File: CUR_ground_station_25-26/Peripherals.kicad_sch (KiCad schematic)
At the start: 0 parts

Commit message: added user stuff
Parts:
- added BZ1: CMT-1209-390T, symbol Device:Buzzer
- added D1: D_Schottky, symbol Device:D_Schottky
- added Led_1, Led_2, Led_3: CLV1L-FKB, LED_SMD:LED_Cree-PLCC4_3.2x2.8mm_CCW, symbol LED:CLV1L-FKB
- added Q1: NTR4003N, symbol Transistor_FET:Q_NMOS_GSD
- added R1, R10, R11, R2, R7, R8: 22, symbol Device:R_Small_US
- added R3, R5, R6, R9: 150, symbol Device:R_Small_US
- added R4: 10k, symbol Device:R_Small_US
- added SW1, SW2, SW3, SW4: SW_Push, symbol Switch:SW_Push
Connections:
- new net: Led_3.2 (RK), R9.1
- new net: Led_1.4 (BK), R2.1
- new net: Led_3.3 (GK), R10.1
- new net: Led_3.4 (BK), R11.1
- new net: Led_2.2 (RK), R6.1
- new net: Q1.1 (G), R4.1, R5.2
- new net: BZ1.2 (-), D1.2 (A), Q1.3 (D)
- new net: Led_2.4 (BK), R8.1
- new net: Led_2.3 (GK), R7.1
- new net: Led_1.2 (RK), R3.1
- new net: Led_1.3 (GK), R1.1
- new net +3V3: BZ1.1 (+), D1.1 (K), Led_1.1 (A), Led_2.1 (A), Led_3.1 (A), SW1.2, SW2.2, SW3.2, SW4.2
- new net BTN_1: SW1.1, SW2.1, SW3.1, SW4.1
- new net Buzzer: R5.1
- new net GND: Q1.2 (S), R4.2
- new net LED_1_B: R2.2
- new net LED_1_G: R1.2
- new net LED_1_R: R3.2
- new net LED_2_B: R8.2
- new net LED_2_G: R7.2
- new net LED_2_R: R6.2
- new net LED_3_B: R11.2
- new net LED_3_G: R10.2
- new net LED_3_R: R9.2
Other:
- note added: "Aiming for around 5ma"
- note added: "Blue: 3.1"
- note added: "Button"
- note added: "Buzzer"
- note added: "Forward Voltages"
- note added: "Green: 3.1"
- note added: "LED"
- note added: "Red: 2.6"

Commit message: added buncha stuff from flight computer
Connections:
- net BTN_1: no longer SW2.1, SW3.1, SW4.1
- new net BTN_2: SW2.1
- new net BTN_3: SW3.1
- new net BTN_4: SW4.1
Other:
- moved on the sheet: BZ1, D1, Led_1, Led_2, Led_3, Q1, R1, R10, R11, R2, R3, R4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

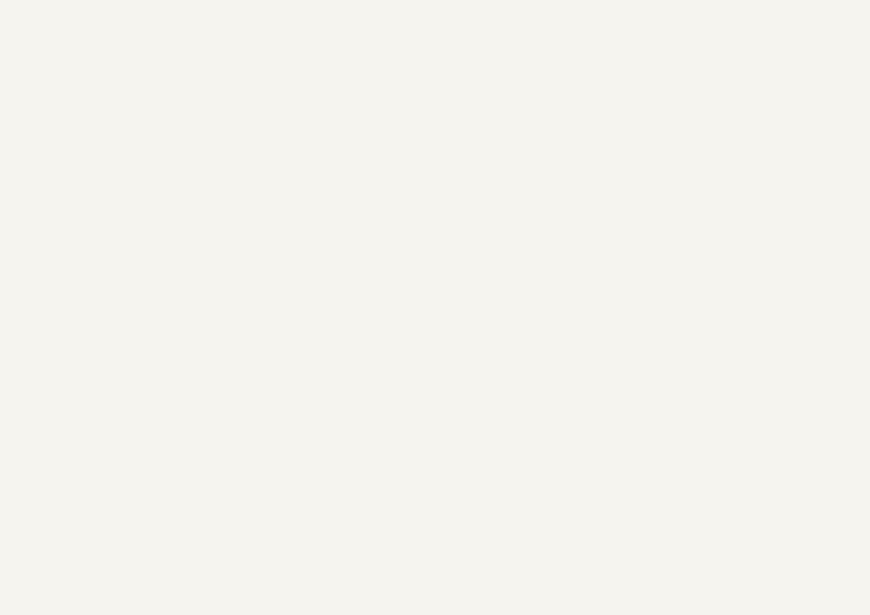
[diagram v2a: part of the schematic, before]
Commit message: Add epaper
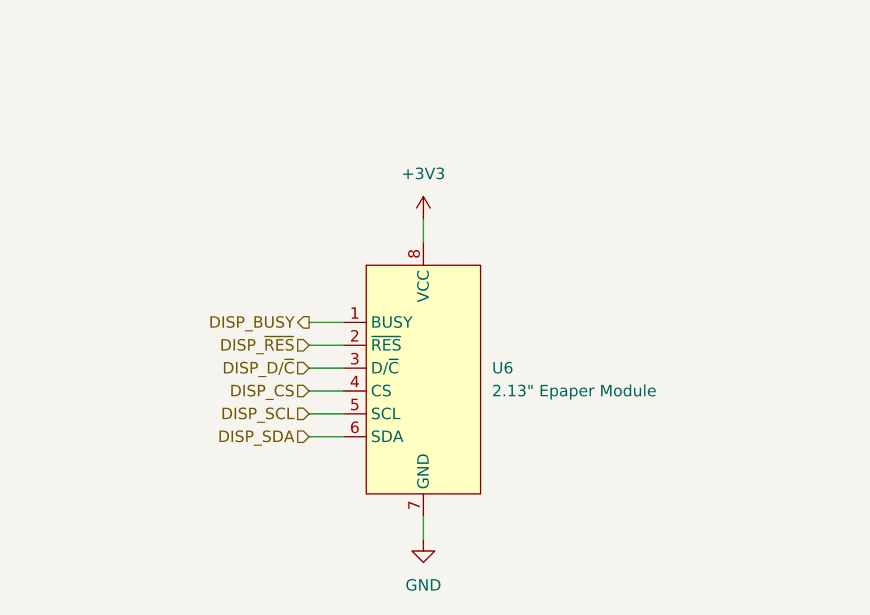
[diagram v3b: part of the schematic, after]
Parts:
- added U6: 2.13" Epaper Module, WeAct-Studio-2.13-Epaper:WeAct-Studio-2.13-Epaper, symbol WeAct-Studio-Epaper:WeAct-Studio-2.13-Epaper
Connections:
- net +3V3: now also U6.8 (VCC)
- net GND: now also U6.7 (GND)
- new net DISP_BUSY: U6.1 (BUSY)
- new net DISP_CS: U6.4 (CS)
- new net DISP_D/~{C}: U6.3 (D/~{C})
- new net DISP_SCL: U6.5 (SCL)
- new net DISP_SDA: U6.6 (SDA)
- new net DISP_~{RES}: U6.2 (~{RES})

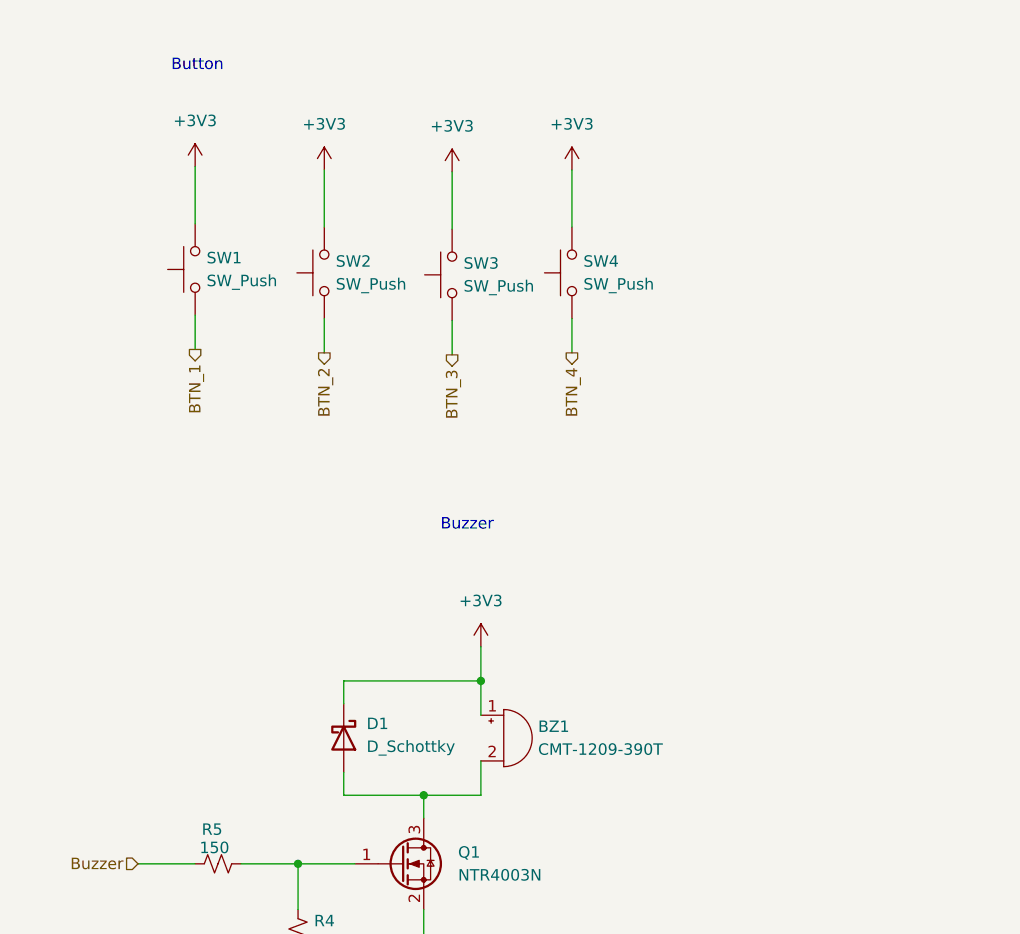
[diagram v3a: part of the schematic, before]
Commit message: Cleanup UI sheet
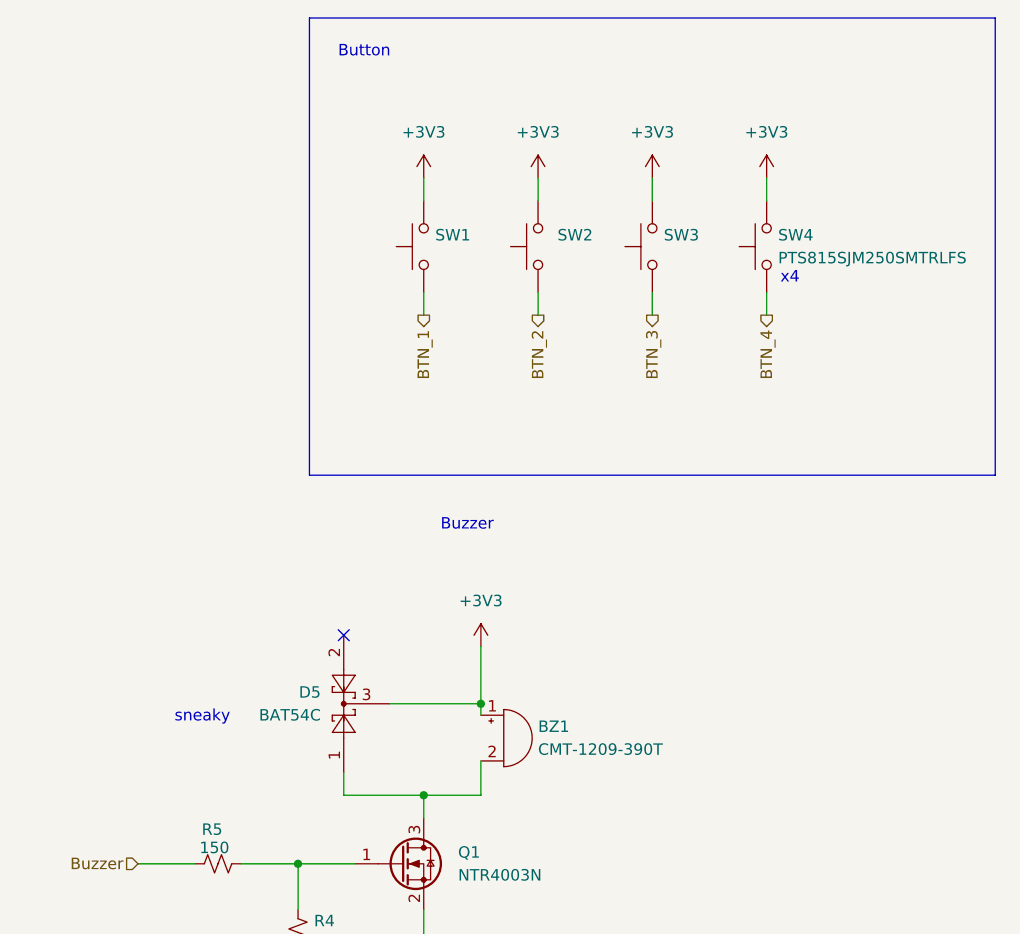
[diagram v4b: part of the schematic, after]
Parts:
- removed D1: D_Schottky, symbol Device:D_Schottky
- added D5: BAT54C, Package_TO_SOT_SMD:SOT-23, symbol Diode:BAT54C
- SW1, SW2, SW3, SW4: value SW_Push -> PTS815SJM250SMTRLFS
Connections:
- net +3V3: now also D5.3
- net at BZ1.2 (-), Q1.3 (D): now also D5.1
- no-connect marks 0 -> 1
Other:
- note added: "sneaky"
- note added: "x4"
- moved on the sheet: SW1, SW2, SW3, SW4

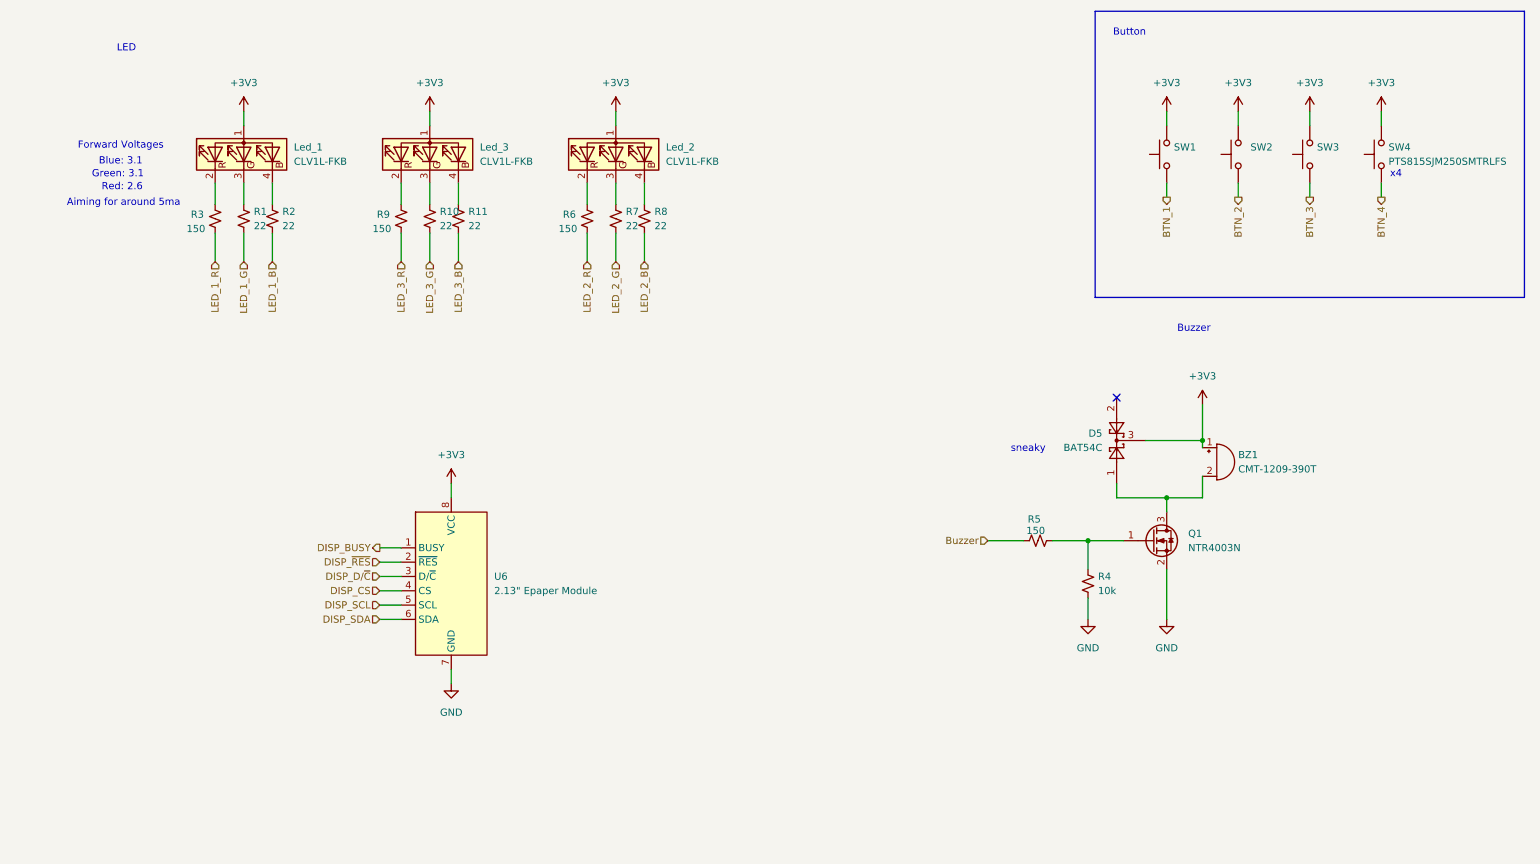
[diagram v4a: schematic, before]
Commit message: Cleanup peripherals again
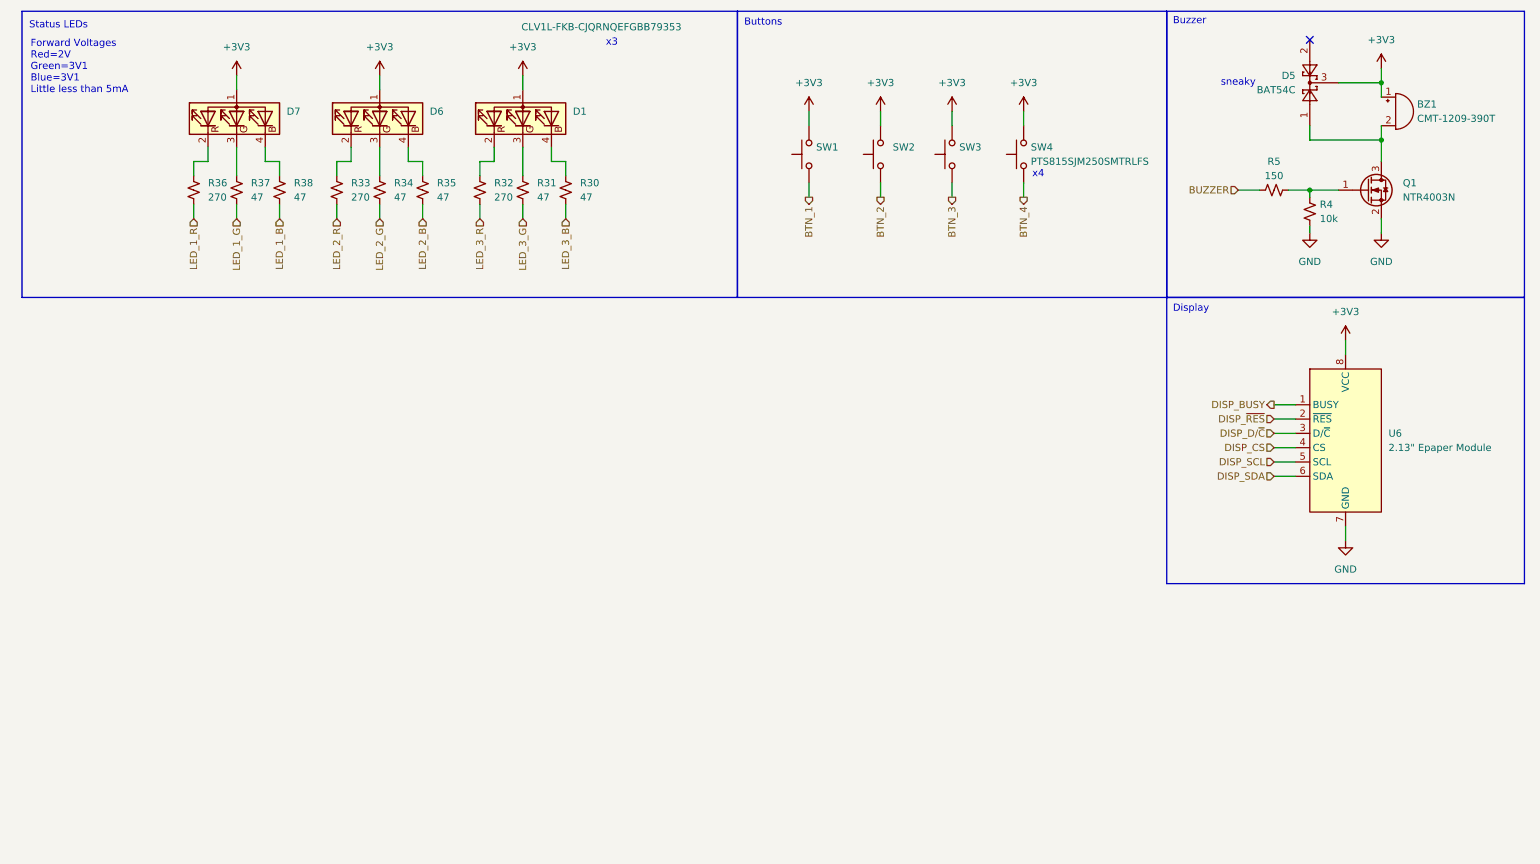
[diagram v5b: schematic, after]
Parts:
- removed Led_1, Led_2, Led_3: CLV1L-FKB, LED_SMD:LED_Cree-PLCC4_3.2x2.8mm_CCW, symbol LED:CLV1L-FKB
- removed R1, R10, R11, R2, R7, R8: 22, symbol Device:R_Small_US
- removed R3, R6, R9: 150, symbol Device:R_Small_US
- added D1, D6, D7: CLV1L-FKB-CJQRNQEFGBB79353, LED_SMD:LED_Cree-PLCC4_3.2x2.8mm_CCW, symbol Device:LED_ARGB
- added R30, R31, R34, R35, R37, R38: 47, symbol Device:R_Small_US
- added R32, R33, R36: 270, symbol Device:R_Small_US
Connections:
- net +3V3: now also D1.1 (A), D6.1 (A), D7.1 (A)
- net LED_1_B: now also R38.2
- net LED_1_G: now also R37.2
- net LED_1_R: now also R36.2
- net LED_2_B: now also R35.2
- net LED_2_G: now also R34.2
- net LED_2_R: now also R33.2
- net LED_3_B: now also R30.2
- net LED_3_G: now also R31.2
- net LED_3_R: now also R32.2
- net Buzzer renamed BUZZER
- new net: D1.4 (BK), R30.1
- new net: D1.2 (RK), R32.1
- new net: D7.2 (RK), R36.1
- new net: D7.3 (GK), R37.1
- new net: D7.4 (BK), R38.1
- new net: D6.3 (GK), R34.1
- new net: D1.3 (GK), R31.1
- new net: D6.4 (BK), R35.1
- new net: D6.2 (RK), R33.1
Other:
- note added: "Buttons"
- note added: "Display"
- note added: "Forward Voltages Red=2V Green=3V1 Blue=3V1 Little less than 5mA"
- note added: "Status LEDs"
- note added: "x3"
- note removed: "Aiming for around 5ma"
- note removed: "Blue: 3.1"
- note removed: "Button"
- note removed: "Forward Voltages"
- note removed: "Green: 3.1"
- note removed: "LED"
- note removed: "Red: 2.6"
- moved on the sheet: BZ1, D5, Q1, R4, R5, SW1, SW2, SW3, SW4, U6

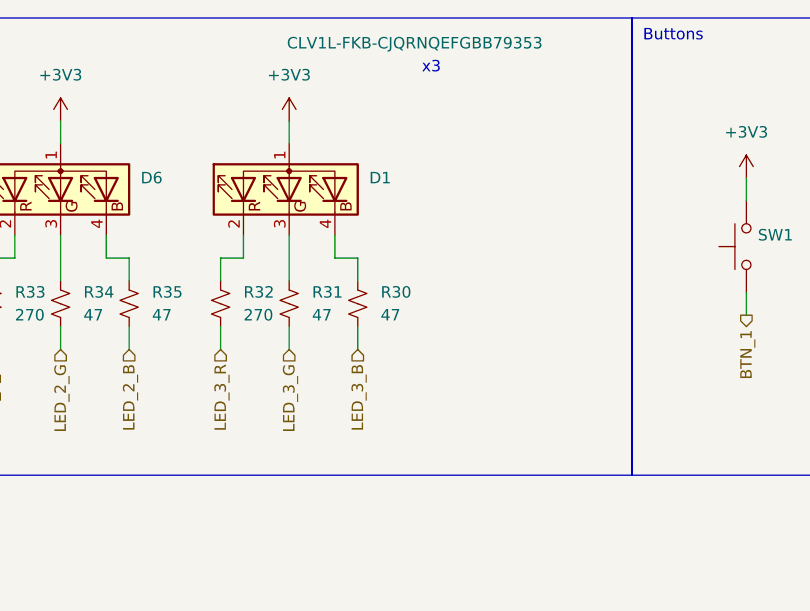
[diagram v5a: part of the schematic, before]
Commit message: Change MCU, hookup more pins
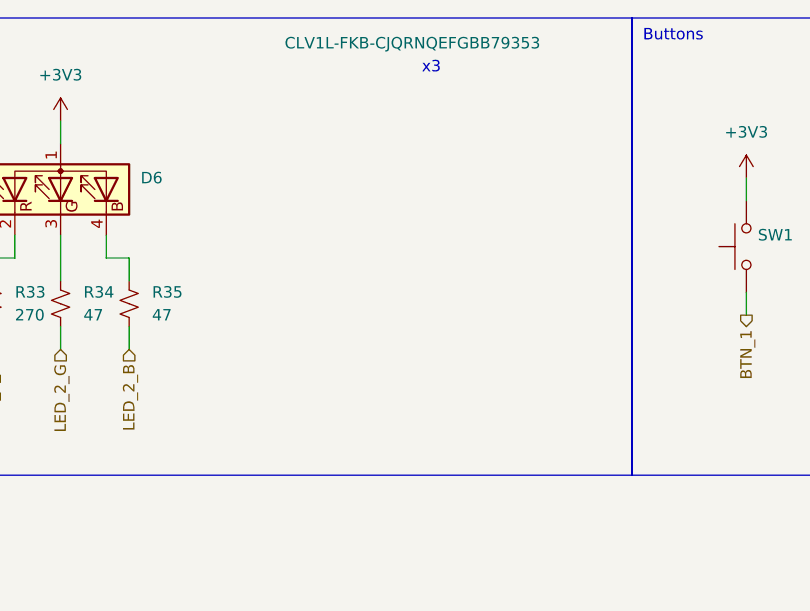
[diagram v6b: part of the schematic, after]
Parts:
- removed D1: CLV1L-FKB-CJQRNQEFGBB79353, LED_SMD:LED_Cree-PLCC4_3.2x2.8mm_CCW, symbol Device:LED_ARGB
- removed R30, R31: 47, symbol Device:R_Small_US
- removed R32: 270, symbol Device:R_Small_US

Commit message: updating footprints
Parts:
- R33, R34, R35, R36, R37, R38, R4, R5: footprint (none) -> Resistor_SMD:R_0603_1608Metric
- SW1, SW2, SW3, SW4: footprint (none) -> PTS815_SJM_250_SMTR_LFS:SW_Push_PTS815_SJM_250_SMTR_LFS
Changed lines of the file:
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@@
 			)
 		)
-		(property "Footprint" ""
+		(property "Footprint" "PTS815_SJM_250_SMTR_LFS:SW_Push_PTS815_SJM_250_SMTR_LFS"
 			(at 160.02 38.1 0)
 			(effects
@@
 			)
 		)
-		(property "Footprint" ""
+		(property "Footprint" "Resistor_SMD:R_0603_1608Metric"
 			(at 234.95 44.45 0)
 			(effects
@@
 			)
 		)
-		(property "Footprint" ""
+		(property "Footprint" "Resistor_SMD:R_0603_1608Metric"
 			(at 76.2 44.45 0)
 			(effects
@@
 			)
 		)
-		(property "Footprint" ""
+		(property "Footprint" "Resistor_SMD:R_0603_1608Metric"
 			(at 58.42 44.45 0)
 			(effects
@@
 			)
 		)
-		(property "Footprint" ""
+		(property "Footprint" "Resistor_SMD:R_0603_1608Metric"
 			(at 50.8 44.45 0)
 			(effects
@@
 			)
 		)
-		(property "Footprint" ""
+		(property "Footprint" "PTS815_SJM_250_SMTR_LFS:SW_Push_PTS815_SJM_250_SMTR_LFS"
 			(at 185.42 38.1 0)
 			(effects
@@
 			)
 		)
-		(property "Footprint" ""
+		(property "Footprint" "PTS815_SJM_250_SMTR_LFS:SW_Push_PTS815_SJM_250_SMTR_LFS"
 			(at 147.32 38.1 0)
 			(effects
@@
 			)
 		)
-		(property "Footprint" ""
+		(property "Footprint" "Resistor_SMD:R_0603_1608Metric"
 			(at 83.82 44.45 0)
 			(effects
@@
 			)
 		)
-		(property "Footprint" ""
+		(property "Footprint" "Resistor_SMD:R_0603_1608Metric"
 			(at 43.18 44.45 0)
 			(effects
@@
 			)
 		)
-		(property "Footprint" ""
+		(property "Footprint" "Resistor_SMD:R_0603_1608Metric"
 			(at 241.3 48.26 0)
 			(effects
@@
 			)
 		)
-		(property "Footprint" ""
+		(property "Footprint" "PTS815_SJM_250_SMTR_LFS:SW_Push_PTS815_SJM_250_SMTR_LFS"
 			(at 172.72 38.1 0)
 			(effects
@@
 			)
 		)
-		(property "Footprint" ""
+		(property "Footprint" "Resistor_SMD:R_0603_1608Metric"
 			(at 68.58 44.45 0)
 			(effects

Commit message: added more footprints
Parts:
- BZ1: footprint (none) -> Buzzer_SameSky:XDCR_CMT-7525-03-SMT-TR
- Q1: footprint (none) -> Package_TO_SOT_SMD:SOT-23
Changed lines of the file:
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@@
 			)
 		)
-		(property "Footprint" ""
+		(property "Footprint" "Package_TO_SOT_SMD:SOT-23"
 			(at 256.54 41.91 0)
 			(effects
@@
 			)
 		)
-		(property "Footprint" ""
+		(property "Footprint" "Buzzer_SameSky:XDCR_CMT-7525-03-SMT-TR"
 			(at 255.905 27.94 90)
 			(effects
